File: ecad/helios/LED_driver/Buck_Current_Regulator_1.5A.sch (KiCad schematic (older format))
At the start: 19 parts, among them U2 TPS92512

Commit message: Improves the layout
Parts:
- L1: footprint Inductors_SMD:L_Wuerth_WE-PD-Typ-LS -> FORT:7447709101
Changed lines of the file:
@@
 AR Path="/5AA2AB58/5AA2AC23" Ref="U2"  Part="1"
 AR Path="/5AA6DCFC/5AA2AC23" Ref="U3"  Part="1"
-F 0 "U2" H 6100 3150 60  0000 C CNN
+F 0 "U3" H 6100 3150 60  0000 C CNN
 F 1 "TPS92512" H 6250 2000 60  0000 C CNN
 F 2 "FORT:PDSO-10-1EP-3x3mm-Pitch0.5mm" H 6150 2550 60  0001 C CNN
@@
 AR Path="/5AA2AB58/5AA7001C" Ref="C8"  Part="1"
 AR Path="/5AA6DCFC/5AA7001C" Ref="C18"  Part="1"
-F 0 "C8" H 2125 2650 50  0000 L CNN
+F 0 "C18" H 2125 2650 50  0000 L CNN
 F 1 "4.7uF,50V" H 2125 2450 50  0000 L CNN
 F 2 "Capacitors_SMD:C_1206" H 2138 2400 50  0001 C CNN
@@
 AR Path="/5AA2AB58/5AA2B956" Ref="L1"  Part="1"
 AR Path="/5AA6DCFC/5AA2B956" Ref="L2"  Part="1"
-F 0 "L1" V 8100 2250 50  0000 C CNN
+F 0 "L2" V 8100 2250 50  0000 C CNN
 F 1 "100uH, 2.5A" V 7950 2250 50  0000 C CNN
-F 2 "Inductors_SMD:L_Wuerth_WE-PD-Typ-LS" H 8000 2250 50  0001 C CNN
+F 2 "FORT:7447709101" H 8000 2250 50  0001 C CNN
 F 3 "" H 8000 2250 50  0001 C CNN
 F 4 "7447709101" H 8000 2250 60  0001 C CNN "Part Number"
@@
 AR Path="/5AA2AB58/5AA7001E" Ref="D2"  Part="1"
 AR Path="/5AA6DCFC/5AA7001E" Ref="D4"  Part="1"
-F 0 "D2" H 7800 2800 50  0000 C CNN
+F 0 "D4" H 7800 2800 50  0000 C CNN
 F 1 "60V, 2A" H 7800 2600 50  0000 C CNN
 F 2 "Diodes_SMD:D_SMB" H 7800 2700 50  0001 C CNN
@@
 AR Path="/5AA2AB58/5AA7001F" Ref="D1"  Part="1"
 AR Path="/5AA6DCFC/5AA7001F" Ref="D3"  Part="1"
-F 0 "D1" H 7100 1700 50  0000 C CNN
+F 0 "D3" H 7100 1700 50  0000 C CNN
 F 1 "60V, 2A" H 7100 1500 50  0000 C CNN
 F 2 "Diodes_SMD:D_SMB" H 7100 1600 50  0001 C CNN
@@
 $EndComp
 $Comp
-L GND #PWR016
+L GND #PWR020
 U 1 1 5AA70020
 P 8400 3750
-AR Path="/5AA2AB58/5AA70020" Ref="#PWR016"  Part="1"
-AR Path="/5AA6DCFC/5AA70020" Ref="#PWR018"  Part="1"
-F 0 "#PWR016" H 8400 3500 50  0001 C CNN
+AR Path="/5AA2AB58/5AA70020" Ref="#PWR020"  Part="1"
+AR Path="/5AA6DCFC/5AA70020" Ref="#PWR022"  Part="1"
+F 0 "#PWR022" H 8400 3500 50  0001 C CNN
 F 1 "GND" H 8400 3600 50  0000 C CNN
 F 2 "" H 8400 3750 50  0001 C CNN
@@
 AR Path="/5AA2AB58/5AA70021" Ref="R9"  Part="1"
 AR Path="/5AA6DCFC/5AA70021" Ref="R16"  Part="1"
-F 0 "R9" V 7280 2600 50  0000 C CNN
+F 0 "R16" V 7280 2600 50  0000 C CNN
 F 1 "1K" V 7200 2600 50  0000 C CNN
 F 2 "Resistors_SMD:R_0603" V 7130 2600 50  0001 C CNN
@@
 AR Path="/5AA2AB58/5AA70022" Ref="R13"  Part="1"
 AR Path="/5AA6DCFC/5AA70022" Ref="R20"  Part="1"
-F 0 "R13" V 8480 3350 50  0000 C CNN
+F 0 "R20" V 8480 3350 50  0000 C CNN
 F 1 "0.2, 1%, 0.5W" H 8700 3200 50  0000 C CNN
 F 2 "Resistors_SMD:R_1206" V 8330 3350 50  0001 C CNN
@@
 AR Path="/5AA2AB58/5AA70023" Ref="R8"  Part="1"
 AR Path="/5AA6DCFC/5AA70023" Ref="R15"  Part="1"
-F 0 "R8" V 5580 2250 50  0000 C CNN
+F 0 "R15" V 5580 2250 50  0000 C CNN
 F 1 "10M" V 5500 2250 50  0000 C CNN
 F 2 "Resistors_SMD:R_0603" V 5430 2250 50  0001 C CNN
@@
 AR Path="/5AA2AB58/5AA70024" Ref="R7"  Part="1"
 AR Path="/5AA6DCFC/5AA70024" Ref="R14"  Part="1"
-F 0 "R7" V 4530 2250 50  0000 C CNN
+F 0 "R14" V 4530 2250 50  0000 C CNN
 F 1 "1.96M" V 4450 2250 50  0000 C CNN
 F 2 "Resistors_SMD:R_0603" V 4380 2250 50  0001 C CNN
@@
 AR Path="/5AA2AB58/5AA70025" Ref="R10"  Part="1"
 AR Path="/5AA6DCFC/5AA70025" Ref="R17"  Part="1"
-F 0 "R10" V 4530 2750 50  0000 C CNN
+F 0 "R17" V 4530 2750 50  0000 C CNN
 F 1 "66.5k" V 4450 2750 50  0000 C CNN
 F 2 "Resistors_SMD:R_0603" V 4380 2750 50  0001 C CNN
@@
 AR Path="/5AA2AB58/5AA69587" Ref="R11"  Part="1"
 AR Path="/5AA6DCFC/5AA69587" Ref="R18"  Part="1"
-F 0 "R11" V 5430 3200 50  0000 C CNN
+F 0 "R18" V 5430 3200 50  0000 C CNN
 F 1 "267k" V 5350 3200 50  0000 C CNN
 F 2 "Resistors_SMD:R_0603" V 5280 3200 50  0001 C CNN
@@
 	5350 2950 5800 2950
 $Comp
-L GND #PWR017
+L GND #PWR021
 U 1 1 5AA69658
 P 5350 3500
-AR Path="/5AA2AB58/5AA69658" Ref="#PWR017"  Part="1"
-AR Path="/5AA6DCFC/5AA69658" Ref="#PWR019"  Part="1"
-F 0 "#PWR017" H 5350 3250 50  0001 C CNN
+AR Path="/5AA2AB58/5AA69658" Ref="#PWR021"  Part="1"
+AR Path="/5AA6DCFC/5AA69658" Ref="#PWR023"  Part="1"
+F 0 "#PWR023" H 5350 3250 50  0001 C CNN
 F 1 "GND" H 5350 3350 50  0000 C CNN
 F 2 "" H 5350 3500 50  0001 C CNN
@@
 AR Path="/5AA2AB58/5AA69C44" Ref="C11"  Part="1"
 AR Path="/5AA6DCFC/5AA69C44" Ref="C21"  Part="1"
-F 0 "C11" H 3675 2650 50  0000 L CNN
+F 0 "C21" H 3675 2650 50  0000 L CNN
 F 1 "10nF, 50V" H 3675 2450 50  0000 L CNN
 F 2 "Capacitors_SMD:C_0603" H 3688 2400 50  0001 C CNN
@@
 AR Path="/5AA2AB58/5AA7002B" Ref="C14"  Part="1"
 AR Path="/5AA6DCFC/5AA7002B" Ref="C24"  Part="1"
-F 0 "C14" H 4875 3200 50  0000 L CNN
+F 0 "C24" H 4875 3200 50  0000 L CNN
 F 1 "100nF" H 4875 3000 50  0000 L CNN
 F 2 "Capacitors_SMD:C_0603" H 4888 2950 50  0001 C CNN
@@
 AR Path="/5AA2AB58/5AA6A967" Ref="C9"  Part="1"
 AR Path="/5AA6DCFC/5AA6A967" Ref="C19"  Part="1"
-F 0 "C9" H 2675 2650 50  0000 L CNN
+F 0 "C19" H 2675 2650 50  0000 L CNN
 F 1 "4.7uF,50V" H 2675 2450 50  0000 L CNN
 F 2 "Capacitors_SMD:C_1206" H 2688 2400 50  0001 C CNN
@@
 AR Path="/5AA2AB58/5AA6A9D1" Ref="C10"  Part="1"
 AR Path="/5AA6DCFC/5AA6A9D1" Ref="C20"  Part="1"
-F 0 "C10" H 3175 2650 50  0000 L CNN
+F 0 "C20" H 3175 2650 50  0000 L CNN
 F 1 "4.7uF,50V" H 3175 2450 50  0000 L CNN
 F 2 "Capacitors_SMD:C_1206" H 3188 2400 50  0001 C CNN
@@
 AR Path="/5AA2AB58/5AA7002E" Ref="C6"  Part="1"
 AR Path="/5AA6DCFC/5AA7002E" Ref="C16"  Part="1"
-F 0 "C6" V 7350 2150 50  0000 L CNN
+F 0 "C16" V 7350 2150 50  0000 L CNN
 F 1 "100nF" V 7100 1950 50  0000 L CNN
 F 2 "Capacitors_SMD:C_0603" H 7288 1900 50  0001 C CNN
@@
 AR Path="/5AA2AB58/5AA6B735" Ref="C12"  Part="1"
 AR Path="/5AA6DCFC/5AA6B735" Ref="C22"  Part="1"
-F 0 "C12" H 8425 2750 50  0000 L CNN
+F 0 "C22" H 8425 2750 50  0000 L CNN
 F 1 "4.7uF,50V" H 8425 2550 50  0000 L CNN
 F 2 "Capacitors_SMD:C_1206" H 8438 2500 50  0001 C CNN
@@
 AR Path="/5AA2AB58/5AAA9295" Ref="C7"  Part="1"
 AR Path="/5AA6DCFC/5AAA9295" Ref="C17"  Part="1"
-F 0 "C7" H 1775 2650 50  0000 L CNN
+F 0 "C17" H 1775 2650 50  0000 L CNN
 F 1 "4.7uF,50V" H 1775 2450 50  0000 L CNN
 F 2 "Capacitors_SMD:C_1206" H 1788 2400 50  0001 C CNN
@@
 AR Path="/5AA2AB58/5AAA9C17" Ref="C13"  Part="1"
 AR Path="/5AA6DCFC/5AAA9C17" Ref="C23"  Part="1"
-F 0 "C13" H 8975 2750 50  0000 L CNN
+F 0 "C23" H 8975 2750 50  0000 L CNN
 F 1 "4.7uF,50V" H 8975 2550 50  0000 L CNN
 F 2 "Capacitors_SMD:C_1206" H 8988 2500 50  0001 C CNN

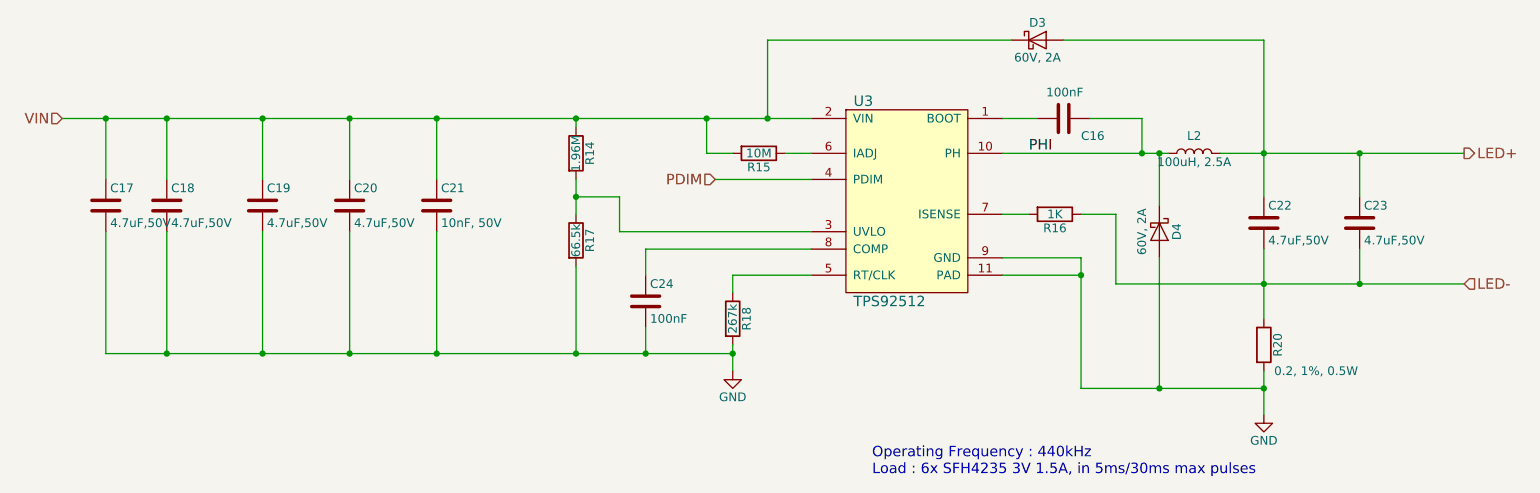
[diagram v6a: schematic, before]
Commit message: Updates BOM of Helios LED Driver
Missed out the change for 1/10 of power illumination
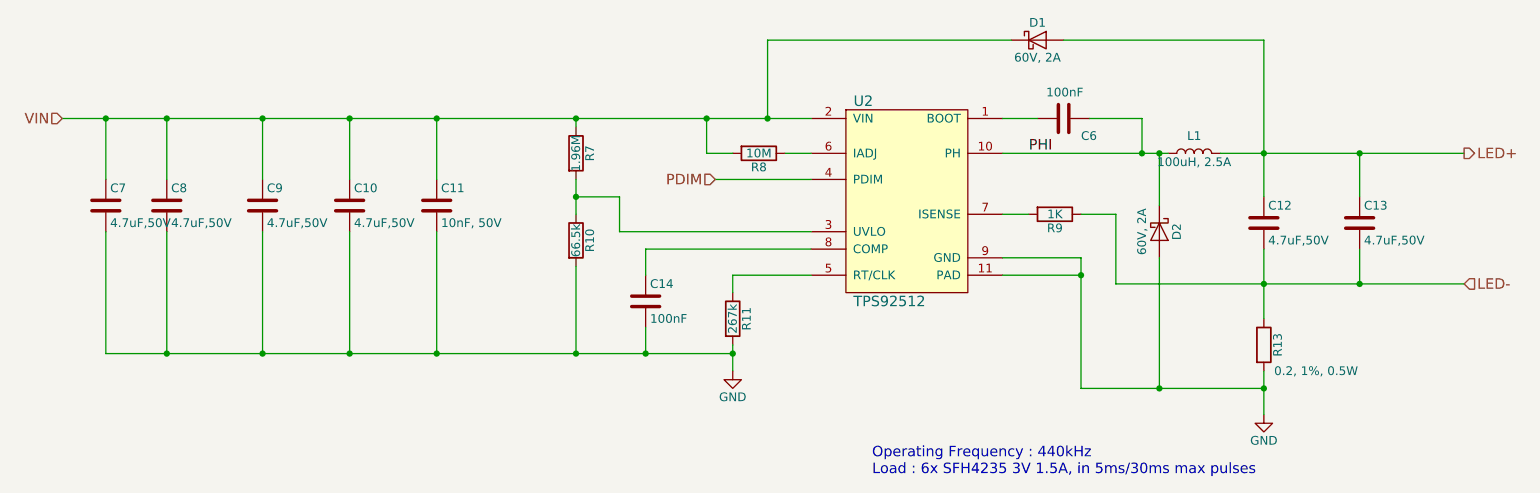
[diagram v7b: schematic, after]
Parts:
- U2: Part Number TPS92512 -> TPS92512DGQR
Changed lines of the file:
@@
 $Descr A4 11693 8268
 encoding utf-8
-Sheet 3 6
+Sheet 2 6
 Title ""
 Date ""
@@
 AR Path="/5AA2AB58/5AA2AC23" Ref="U2"  Part="1"
 AR Path="/5AA6DCFC/5AA2AC23" Ref="U3"  Part="1"
-F 0 "U3" H 6100 3150 60  0000 C CNN
+F 0 "U2" H 6100 3150 60  0000 C CNN
 F 1 "TPS92512" H 6250 2000 60  0000 C CNN
 F 2 "FORT:PDSO-10-1EP-3x3mm-Pitch0.5mm" H 6150 2550 60  0001 C CNN
 F 3 "" H 6150 2550 60  0001 C CNN
-F 4 "TPS92512" H 6350 2550 60  0001 C CNN "Part Number"
+F 4 "TPS92512DGQR" H 6350 2550 60  0001 C CNN "Part Number"
 	1    6350 2550
 	1    0    0    -1
@@
 AR Path="/5AA2AB58/5AA7001C" Ref="C8"  Part="1"
 AR Path="/5AA6DCFC/5AA7001C" Ref="C18"  Part="1"
-F 0 "C18" H 2125 2650 50  0000 L CNN
+F 0 "C8" H 2125 2650 50  0000 L CNN
 F 1 "4.7uF,50V" H 2125 2450 50  0000 L CNN
 F 2 "Capacitors_SMD:C_1206" H 2138 2400 50  0001 C CNN
@@
 AR Path="/5AA2AB58/5AA2B956" Ref="L1"  Part="1"
 AR Path="/5AA6DCFC/5AA2B956" Ref="L2"  Part="1"
-F 0 "L2" V 8100 2250 50  0000 C CNN
+F 0 "L1" V 8100 2250 50  0000 C CNN
 F 1 "100uH, 2.5A" V 7950 2250 50  0000 C CNN
 F 2 "FORT:7447709101" H 8000 2250 50  0001 C CNN
@@
 AR Path="/5AA2AB58/5AA7001E" Ref="D2"  Part="1"
 AR Path="/5AA6DCFC/5AA7001E" Ref="D4"  Part="1"
-F 0 "D4" H 7800 2800 50  0000 C CNN
+F 0 "D2" H 7800 2800 50  0000 C CNN
 F 1 "60V, 2A" H 7800 2600 50  0000 C CNN
 F 2 "Diodes_SMD:D_SMB" H 7800 2700 50  0001 C CNN
@@
 AR Path="/5AA2AB58/5AA7001F" Ref="D1"  Part="1"
 AR Path="/5AA6DCFC/5AA7001F" Ref="D3"  Part="1"
-F 0 "D3" H 7100 1700 50  0000 C CNN
+F 0 "D1" H 7100 1700 50  0000 C CNN
 F 1 "60V, 2A" H 7100 1500 50  0000 C CNN
 F 2 "Diodes_SMD:D_SMB" H 7100 1600 50  0001 C CNN
@@
 $EndComp
 $Comp
-L GND #PWR24
+L GND #PWR023
 U 1 1 5AA70020
 P 8400 3750
-AR Path="/5AA2AB58/5AA70020" Ref="#PWR24"  Part="1"
-AR Path="/5AA6DCFC/5AA70020" Ref="#PWR26"  Part="1"
-F 0 "#PWR26" H 8400 3500 50  0001 C CNN
+AR Path="/5AA2AB58/5AA70020" Ref="#PWR023"  Part="1"
+AR Path="/5AA6DCFC/5AA70020" Ref="#PWR025"  Part="1"
+F 0 "#PWR023" H 8400 3500 50  0001 C CNN
 F 1 "GND" H 8400 3600 50  0000 C CNN
 F 2 "" H 8400 3750 50  0001 C CNN
@@
 AR Path="/5AA2AB58/5AA70021" Ref="R9"  Part="1"
 AR Path="/5AA6DCFC/5AA70021" Ref="R16"  Part="1"
-F 0 "R16" V 7280 2600 50  0000 C CNN
+F 0 "R9" V 7280 2600 50  0000 C CNN
 F 1 "1K" V 7200 2600 50  0000 C CNN
 F 2 "Resistors_SMD:R_0603" V 7130 2600 50  0001 C CNN
@@
 AR Path="/5AA2AB58/5AA70022" Ref="R13"  Part="1"
 AR Path="/5AA6DCFC/5AA70022" Ref="R20"  Part="1"
-F 0 "R20" V 8480 3350 50  0000 C CNN
+F 0 "R13" V 8480 3350 50  0000 C CNN
 F 1 "0.2, 1%, 0.5W" H 8700 3200 50  0000 C CNN
 F 2 "Resistors_SMD:R_1206" V 8330 3350 50  0001 C CNN
@@
 AR Path="/5AA2AB58/5AA70023" Ref="R8"  Part="1"
 AR Path="/5AA6DCFC/5AA70023" Ref="R15"  Part="1"
-F 0 "R15" V 5580 2250 50  0000 C CNN
+F 0 "R8" V 5580 2250 50  0000 C CNN
 F 1 "10M" V 5500 2250 50  0000 C CNN
 F 2 "Resistors_SMD:R_0603" V 5430 2250 50  0001 C CNN
@@
 AR Path="/5AA2AB58/5AA70024" Ref="R7"  Part="1"
 AR Path="/5AA6DCFC/5AA70024" Ref="R14"  Part="1"
-F 0 "R14" V 4530 2250 50  0000 C CNN
+F 0 "R7" V 4530 2250 50  0000 C CNN
 F 1 "1.96M" V 4450 2250 50  0000 C CNN
 F 2 "Resistors_SMD:R_0603" V 4380 2250 50  0001 C CNN
@@
 AR Path="/5AA2AB58/5AA70025" Ref="R10"  Part="1"
 AR Path="/5AA6DCFC/5AA70025" Ref="R17"  Part="1"
-F 0 "R17" V 4530 2750 50  0000 C CNN
+F 0 "R10" V 4530 2750 50  0000 C CNN
 F 1 "66.5k" V 4450 2750 50  0000 C CNN
 F 2 "Resistors_SMD:R_0603" V 4380 2750 50  0001 C CNN
@@
 AR Path="/5AA2AB58/5AA69587" Ref="R11"  Part="1"
 AR Path="/5AA6DCFC/5AA69587" Ref="R18"  Part="1"
-F 0 "R18" V 5430 3200 50  0000 C CNN
+F 0 "R11" V 5430 3200 50  0000 C CNN
 F 1 "267k" V 5350 3200 50  0000 C CNN
 F 2 "Resistors_SMD:R_0603" V 5280 3200 50  0001 C CNN
@@
 	5350 2950 5800 2950
 $Comp
-L GND #PWR23
+L GND #PWR024
 U 1 1 5AA69658
 P 5350 3500
-AR Path="/5AA2AB58/5AA69658" Ref="#PWR23"  Part="1"
-AR Path="/5AA6DCFC/5AA69658" Ref="#PWR25"  Part="1"
-F 0 "#PWR25" H 5350 3250 50  0001 C CNN
+AR Path="/5AA2AB58/5AA69658" Ref="#PWR024"  Part="1"
+AR Path="/5AA6DCFC/5AA69658" Ref="#PWR026"  Part="1"
+F 0 "#PWR024" H 5350 3250 50  0001 C CNN
 F 1 "GND" H 5350 3350 50  0000 C CNN
 F 2 "" H 5350 3500 50  0001 C CNN
@@
 AR Path="/5AA2AB58/5AA69C44" Ref="C11"  Part="1"
 AR Path="/5AA6DCFC/5AA69C44" Ref="C21"  Part="1"
-F 0 "C21" H 3675 2650 50  0000 L CNN
+F 0 "C11" H 3675 2650 50  0000 L CNN
 F 1 "10nF, 50V" H 3675 2450 50  0000 L CNN
 F 2 "Capacitors_SMD:C_0603" H 3688 2400 50  0001 C CNN
@@
 AR Path="/5AA2AB58/5AA7002B" Ref="C14"  Part="1"
 AR Path="/5AA6DCFC/5AA7002B" Ref="C24"  Part="1"
-F 0 "C24" H 4875 3200 50  0000 L CNN
+F 0 "C14" H 4875 3200 50  0000 L CNN
 F 1 "100nF" H 4875 3000 50  0000 L CNN
 F 2 "Capacitors_SMD:C_0603" H 4888 2950 50  0001 C CNN
@@
 AR Path="/5AA2AB58/5AA6A967" Ref="C9"  Part="1"
 AR Path="/5AA6DCFC/5AA6A967" Ref="C19"  Part="1"
-F 0 "C19" H 2675 2650 50  0000 L CNN
+F 0 "C9" H 2675 2650 50  0000 L CNN
 F 1 "4.7uF,50V" H 2675 2450 50  0000 L CNN
 F 2 "Capacitors_SMD:C_1206" H 2688 2400 50  0001 C CNN
@@
 AR Path="/5AA2AB58/5AA6A9D1" Ref="C10"  Part="1"
 AR Path="/5AA6DCFC/5AA6A9D1" Ref="C20"  Part="1"
-F 0 "C20" H 3175 2650 50  0000 L CNN
+F 0 "C10" H 3175 2650 50  0000 L CNN
 F 1 "4.7uF,50V" H 3175 2450 50  0000 L CNN
 F 2 "Capacitors_SMD:C_1206" H 3188 2400 50  0001 C CNN
@@
 AR Path="/5AA2AB58/5AA7002E" Ref="C6"  Part="1"
 AR Path="/5AA6DCFC/5AA7002E" Ref="C16"  Part="1"
-F 0 "C16" V 7350 2150 50  0000 L CNN
+F 0 "C6" V 7350 2150 50  0000 L CNN
 F 1 "100nF" V 7100 1950 50  0000 L CNN
 F 2 "Capacitors_SMD:C_0603" H 7288 1900 50  0001 C CNN
@@
 AR Path="/5AA2AB58/5AA6B735" Ref="C12"  Part="1"
 AR Path="/5AA6DCFC/5AA6B735" Ref="C22"  Part="1"
-F 0 "C22" H 8425 2750 50  0000 L CNN
+F 0 "C12" H 8425 2750 50  0000 L CNN
 F 1 "4.7uF,50V" H 8425 2550 50  0000 L CNN
 F 2 "Capacitors_SMD:C_1206" H 8438 2500 50  0001 C CNN
@@
 AR Path="/5AA2AB58/5AAA9295" Ref="C7"  Part="1"
 AR Path="/5AA6DCFC/5AAA9295" Ref="C17"  Part="1"
-F 0 "C17" H 1775 2650 50  0000 L CNN
+F 0 "C7" H 1775 2650 50  0000 L CNN
 F 1 "4.7uF,50V" H 1775 2450 50  0000 L CNN
 F 2 "Capacitors_SMD:C_1206" H 1788 2400 50  0001 C CNN
@@
 AR Path="/5AA2AB58/5AAA9C17" Ref="C13"  Part="1"
 AR Path="/5AA6DCFC/5AAA9C17" Ref="C23"  Part="1"
-F 0 "C23" H 8975 2750 50  0000 L CNN
+F 0 "C13" H 8975 2750 50  0000 L CNN
 F 1 "4.7uF,50V" H 8975 2550 50  0000 L CNN
 F 2 "Capacitors_SMD:C_1206" H 8988 2500 50  0001 C CNN

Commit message: Updates board for manufacturing
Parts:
- C10, C12, C13, C7, C8, C9: footprint Capacitors_SMD:C_1206 -> Capacitor_SMD:C_1206_3216Metric; symbol C -> LED_driver-rescue:C
- C11, C14, C6: footprint Capacitors_SMD:C_0603 -> Capacitor_SMD:C_0603_1608Metric; symbol C -> LED_driver-rescue:C
- D1, D2: footprint Diodes_SMD:D_SMB -> Diode_SMD:D_SMB; symbol D_Schottky -> LED_driver-rescue:D_Schottky
- L1: symbol L -> LED_driver-rescue:L
- R10, R11, R7, R8, R9: footprint Resistors_SMD:R_0603 -> Resistor_SMD:R_0603_1608Metric; symbol R -> LED_driver-rescue:R
- R13: footprint Resistors_SMD:R_1206 -> Resistor_SMD:R_1206_3216Metric; symbol R -> LED_driver-rescue:R
- U2: symbol TPS92512 -> LED_driver-rescue:TPS92512
